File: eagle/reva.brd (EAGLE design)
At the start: 89 x 55 mm, 233 parts, among them IC1 LM555D, IC2 74HC174D, J1 TYPE-C-31-M-12, U1 TPS63002DRCR

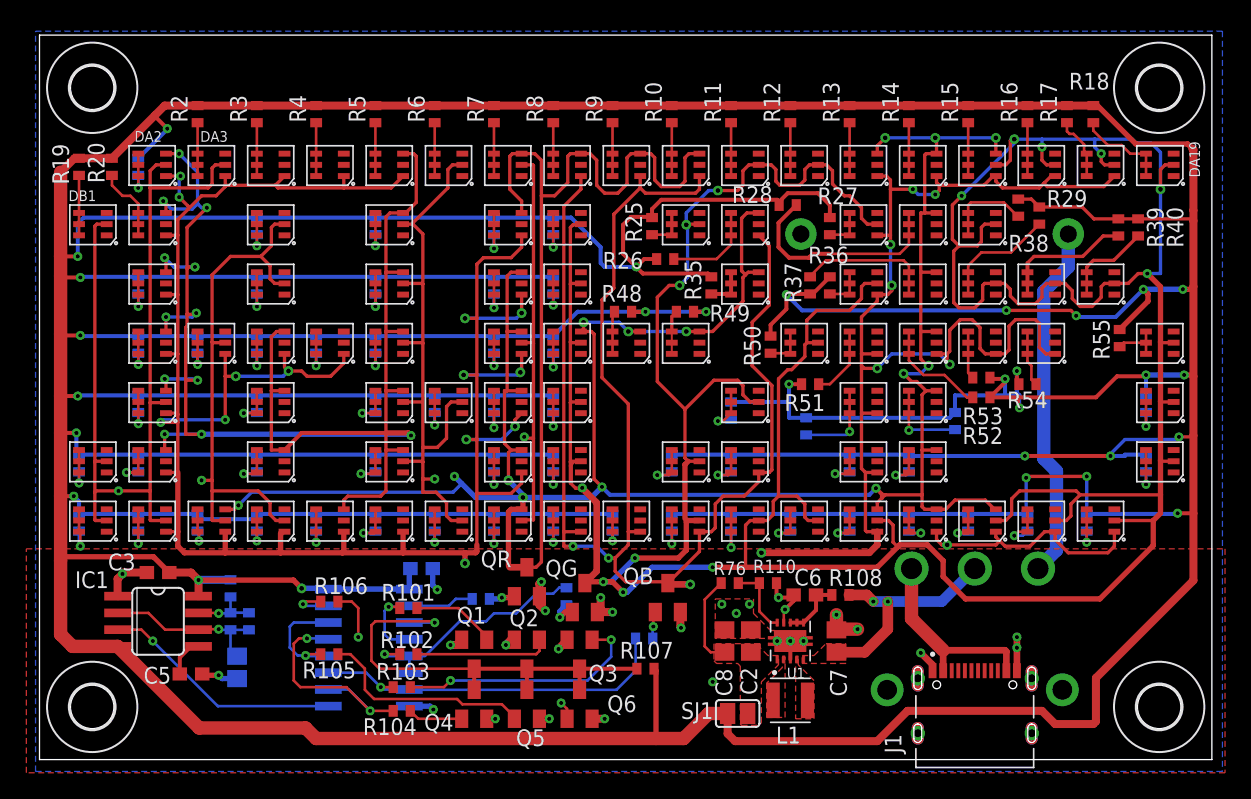
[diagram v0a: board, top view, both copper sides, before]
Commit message: Change pads to 0603 and move some resistors around. This commit marks final draft
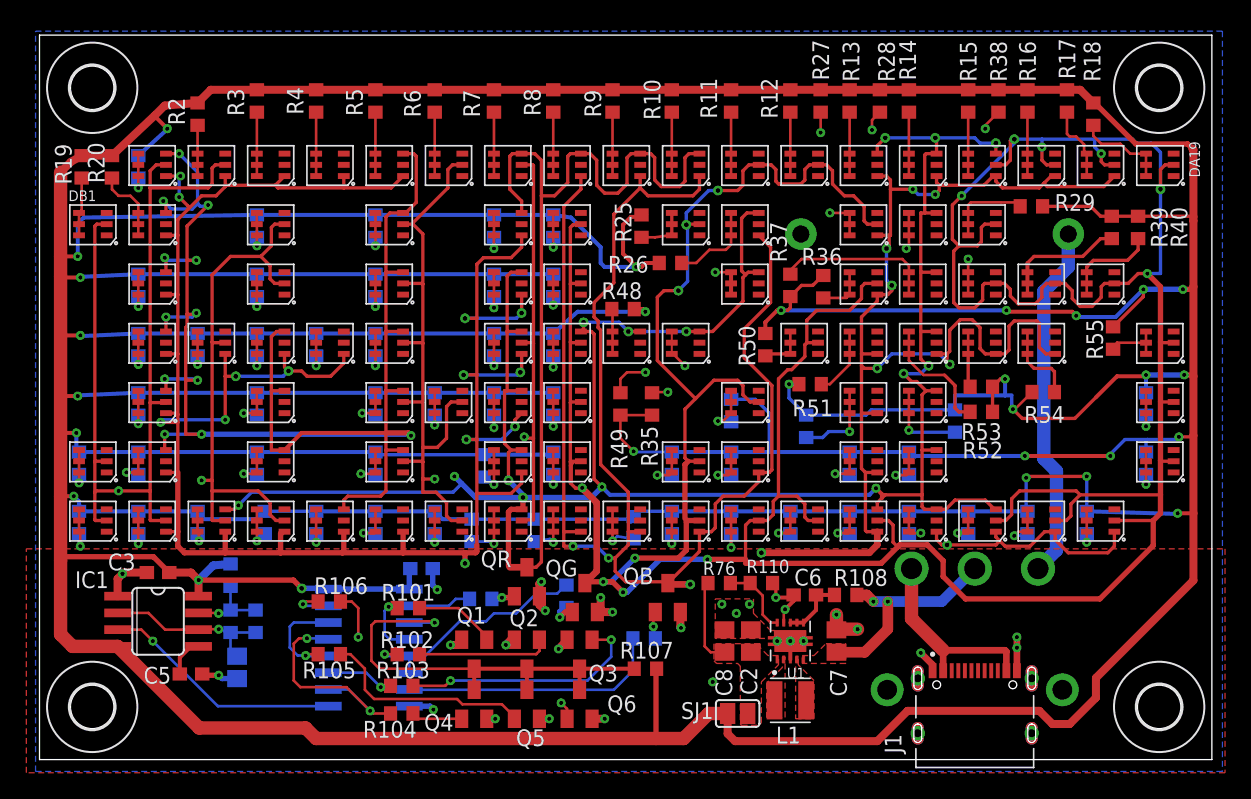
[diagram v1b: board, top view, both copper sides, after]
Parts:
- R1, R10, R100, R101, R102, R103, R104, R105, R106, R107, R108, R109, R11, R110, R12, R13, R14, R15, R16, R17, R18, R19, R2, R20, R21, R22, R23, R24, R25, R26, R27, R28, R29, R3, R30, R31, R32, R33, R34, R35, R36, R37, R38, R39, R4, R40, R41, R42, R43, R44, R45, R46, R47, R48, R49, R5, R50, R51, R52, R53, R54, R55, R56, R57, R58, R59, R6, R60, R61, R62, R63, R64, R65, R66, R67, R68, R69, R7, R70, R71, R72, R73, R74, R75, R76, R77, R78, R79, R8, R80, R81, R82, R83, R84, R85, R86, R87, R88, R89, R9, R90, R91, R92, R93, R94, R95, R96, R97, R98, R99: device adafruit:R0402 -> adafruit:R0603
- U1: value TPS63002DRCR -> TPS63000DRCR
- moved R28 10.6 mm to (63.8, 50.0), turned to 90 degrees
- moved R35 10.1 mm to (46.5, 27.0), turned to 270 degrees
- moved R27 9.53 mm to (59.3, 50.0)
- moved R38 9.24 mm to (72.8, 50.0)
- moved R49 8.54 mm to (44.1, 27.0), turned to 270 degrees
- moved R85 1.80 mm to (32.8, 17.4)
- moved R87 1.65 mm to (45.1, 17.6)
- moved R86 1.52 mm to (37.6, 17.4)
- moved R37 1.50 mm to (57.0, 36.0)
- moved R54 1.34 mm to (76.2, 27.9)
- moved R52 1.10 mm to (71.5, 26.4)
- moved R29 1.00 mm to (75.3, 42.0), turned to 0 degrees
- moved R10 1.00 mm to (48.0, 50.0)
- moved R11 1.00 mm to (52.5, 50.0)
- moved R12 1.00 mm to (57.0, 50.0)
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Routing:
- net +5V: track 788.0 -> 768.2 mm, vias 29 -> 28
- net N$35: track 3.22 -> 16.6 mm, vias 0 -> 2
- net N$27: track 3.22 -> 11.3 mm, vias 0 -> 2
- net N$49: track 3.34 -> 9.44 mm, vias 0 -> 2
- net N$38: track 8.90 -> 14.8 mm, vias 0 -> 2
- net N$28: track 16.8 -> 14.7 mm, vias 0 -> 2
- net N$54: track 4.27 -> 6.21 mm
- net N$37: track 10.4 -> 12.1 mm
- net B-: track 422.0 -> 423.3 mm
- net DIS: track 5.06 -> 6.35 mm
- net N$52: track 8.21 -> 9.46 mm
- net N$87: track 3.15 -> 4.16 mm
- net N$17: track 4.85 -> 5.76 mm
- net N$25: track 3.19 -> 4.03 mm
- net N$85: track 3.55 -> 4.36 mm
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
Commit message: Save
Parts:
- R76: value 680k -> 71k
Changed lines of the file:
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@@
 <grid distance="0.1" unitdist="mm" unit="mm" style="lines" multiple="1" display="yes" altdistance="0.1" altunitdist="mm" altunit="mm"/>
 <layers>
-<layer number="1" name="Top" color="4" fill="1" visible="no" active="yes"/>
-<layer number="2" name="Route2" color="16" fill="1" visible="no" active="yes"/>
+<layer number="1" name="Top" color="4" fill="1" visible="yes" active="yes"/>
+<layer number="2" name="Route2" color="16" fill="1" visible="yes" active="yes"/>
 <layer number="3" name="Route3" color="17" fill="1" visible="no" active="no"/>
 <layer number="4" name="Route4" color="18" fill="1" visible="no" active="no"/>
@@
 <layer number="13" name="Route13" color="21" fill="1" visible="no" active="no"/>
 <layer number="14" name="Route14" color="22" fill="1" visible="no" active="no"/>
-<layer number="15" name="Route15" color="23" fill="1" visible="no" active="yes"/>
+<layer number="15" name="Route15" color="23" fill="1" visible="yes" active="yes"/>
 <layer number="16" name="Bottom" color="1" fill="1" visible="yes" active="yes"/>
 <layer number="17" name="Pads" color="2" fill="1" visible="yes" active="yes"/>
@@
 <layer number="19" name="Unrouted" color="6" fill="1" visible="yes" active="yes"/>
 <layer number="20" name="Dimension" color="24" fill="1" visible="yes" active="yes"/>
-<layer number="21" name="tPlace" color="7" fill="1" visible="no" active="yes"/>
+<layer number="21" name="tPlace" color="7" fill="1" visible="yes" active="yes"/>
 <layer number="22" name="bPlace" color="7" fill="1" visible="yes" active="yes"/>
-<layer number="23" name="tOrigins" color="15" fill="1" visible="no" active="yes"/>
+<layer number="23" name="tOrigins" color="15" fill="1" visible="yes" active="yes"/>
 <layer number="24" name="bOrigins" color="15" fill="1" visible="yes" active="yes"/>
-<layer number="25" name="tNames" color="7" fill="1" visible="no" active="yes"/>
+<layer number="25" name="tNames" color="7" fill="1" visible="yes" active="yes"/>
 <layer number="26" name="bNames" color="7" fill="1" visible="yes" active="yes"/>
 <layer number="27" name="tValues" color="7" fill="1" visible="no" active="yes"/>
@@
 <layer number="37" name="tTest" color="7" fill="1" visible="no" active="yes"/>
 <layer number="38" name="bTest" color="7" fill="1" visible="no" active="yes"/>
-<layer number="39" name="tKeepout" color="4" fill="11" visible="no" active="yes"/>
+<layer number="39" name="tKeepout" color="4" fill="11" visible="yes" active="yes"/>
 <layer number="40" name="bKeepout" color="1" fill="11" visible="yes" active="yes"/>
-<layer number="41" name="tRestrict" color="4" fill="10" visible="no" active="yes"/>
+<layer number="41" name="tRestrict" color="4" fill="10" visible="yes" active="yes"/>
 <layer number="42" name="bRestrict" color="1" fill="10" visible="yes" active="yes"/>
 <layer number="43" name="vRestrict" color="2" fill="10" visible="no" active="yes"/>
@@
 <layer number="49" name="Reference" color="7" fill="1" visible="no" active="yes"/>
 <layer number="50" name="dxf" color="7" fill="1" visible="no" active="yes"/>
-<layer number="51" name="tDocu" color="7" fill="1" visible="no" active="yes"/>
+<layer number="51" name="tDocu" color="7" fill="1" visible="yes" active="yes"/>
 <layer number="52" name="bDocu" color="7" fill="1" visible="yes" active="yes"/>
 <layer number="53" name="tGND_GNDA" color="7" fill="9" visible="no" active="no"/>
@@
 </element>
 <element name="BAT1" library="flashing_ece_2025" package="CR240_CASE" value="CR2450" x="63" y="39.9" smashed="yes" rot="MR180"/>
-<element name="R76" library="adafruit" package="R0603" value="680k" x="51.6" y="13.4" smashed="yes" rot="R180">
+<element name="R76" library="adafruit" package="R0603" value="71k" x="51.6" y="13.4" smashed="yes" rot="R180">
 <attribute name="NAME" x="52.835" y="15.038" size="1.016" layer="25" rot="R180"/>
 <attribute name="VALUE" x="52.235" y="15.432" size="1.27" layer="27" rot="R180"/>
